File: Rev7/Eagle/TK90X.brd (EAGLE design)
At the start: 217.8 x 132.1 mm, 224 parts, among them IC1 Z80, IC10 74LS244N, IC11 LM1886, IC12 LM1889, IC13 4116, IC14 4116, IC15 4116, IC16 4116, IC17 4116, IC18 4116, IC19 4116, IC2 ROM, IC20 4116, IC21 4416, IC22 4416, IC23 4416, IC24 4416, IC25 74LS00, IC26 74LS00, IC27 74LS32, IC28 74LS04, IC29 7805, IC3 ULA TK90, IC4 74LS74, IC5 74LS74, IC6 74LS157, IC7 74LS157, IC8 74LS157, IC9 74LS157, Q1 BC548, Q2 BC548, Q3 BF494, Q4 BC548, Q5 BD139, Q6 BD136, Q7 BC548, Q8 BC517, X1 POWER, X2 EAR, X3 MIC, X4 RCA, X5 RCA, X6 LED, X7 JOYSTICK

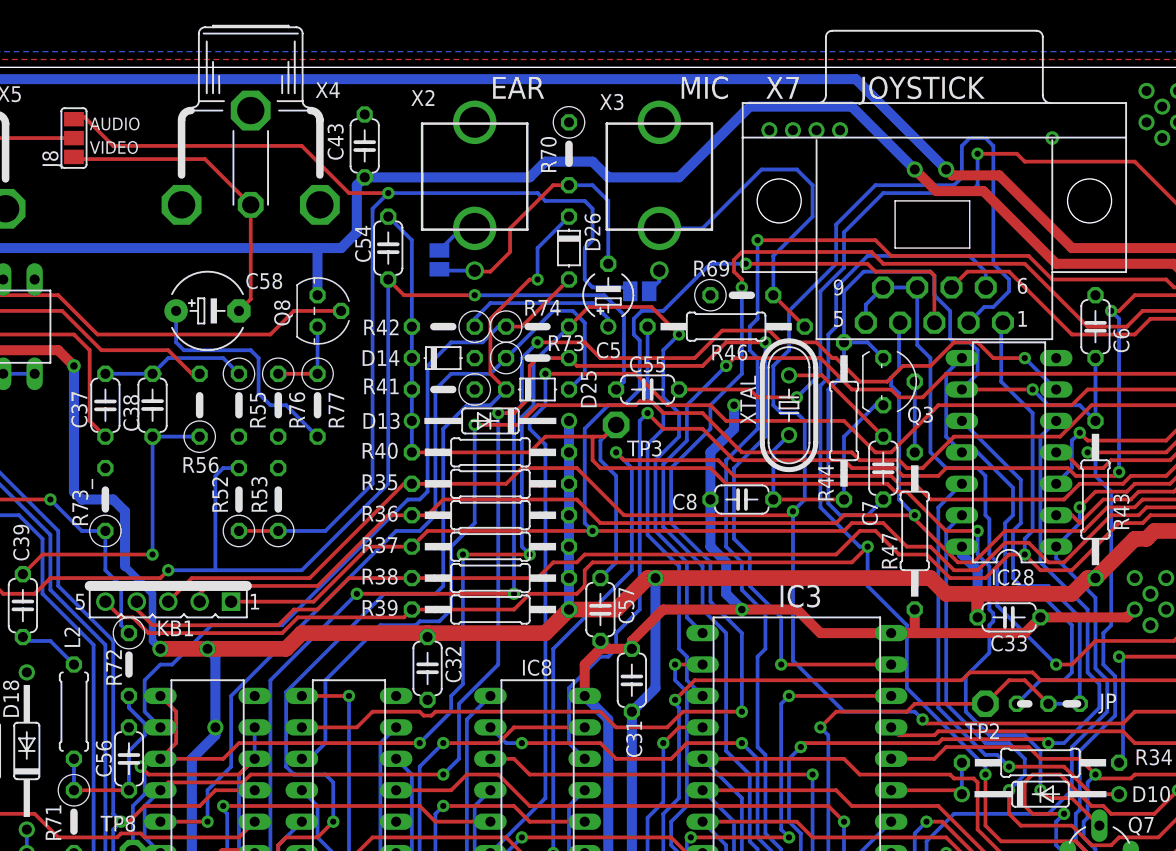
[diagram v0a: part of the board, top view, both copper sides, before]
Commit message: Corrigido valor de R49 e outros pequenos detalhes
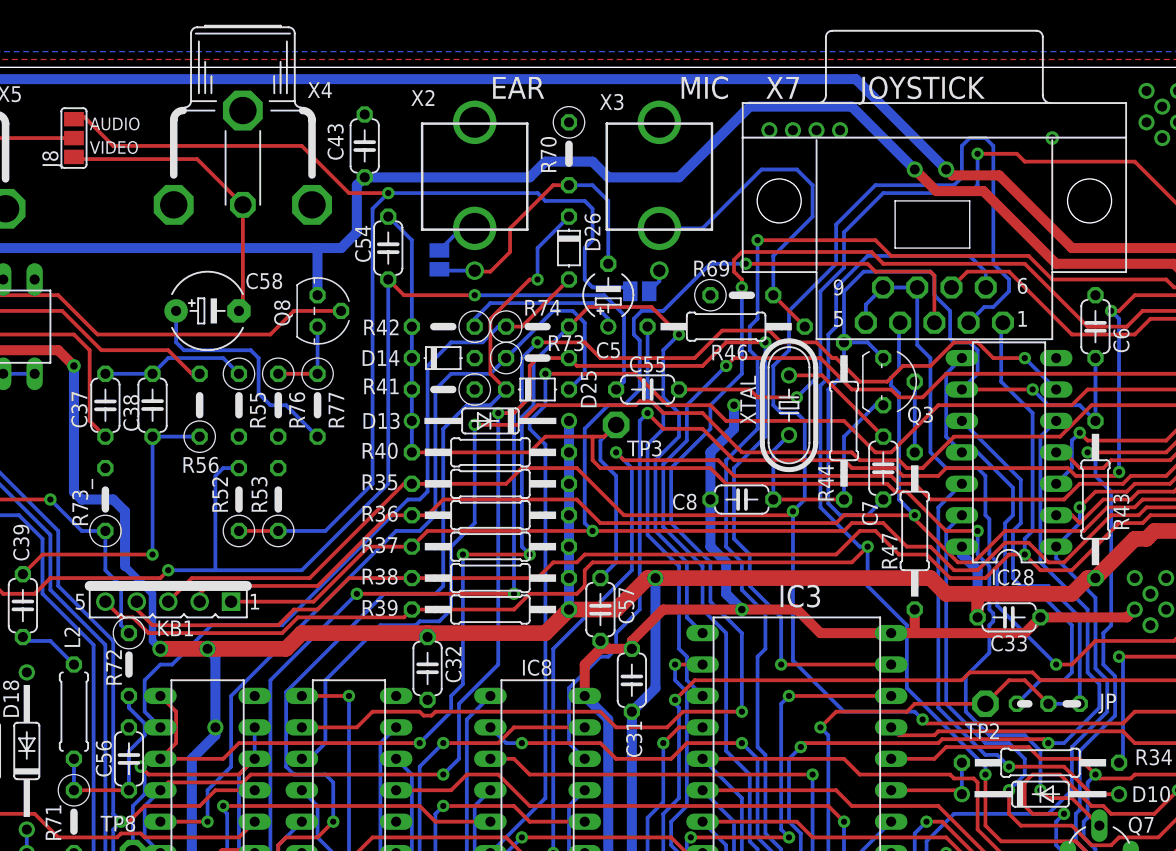
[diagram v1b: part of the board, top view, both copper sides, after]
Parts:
- R49: value 1K -> 4K7
- moved X4 0.64 mm to (42.9, 123.5)
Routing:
- net VIDEO: track 24.9 -> 24.0 mm
- net N$82: track 12.5 -> 11.8 mm

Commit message: Pequenas correções
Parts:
- C1: value 10V100u -> 10V1000u
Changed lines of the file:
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@@
 </autorouter>
 <elements>
-<element name="C1" library="rcl" package="E5-5" value="10V100u" x="203.2" y="83.82" smashed="yes" rot="R90">
+<element name="C1" library="rcl" package="E5-5" value="10V1000u" x="203.2" y="83.82" smashed="yes" rot="R90">
 <attribute name="NAME" x="202.5777" y="88.9635" size="1.27" layer="25" ratio="10"/>
 <attribute name="VALUE" x="206.2226" y="81.3054" size="1.27" layer="27" ratio="10" rot="R90"/>

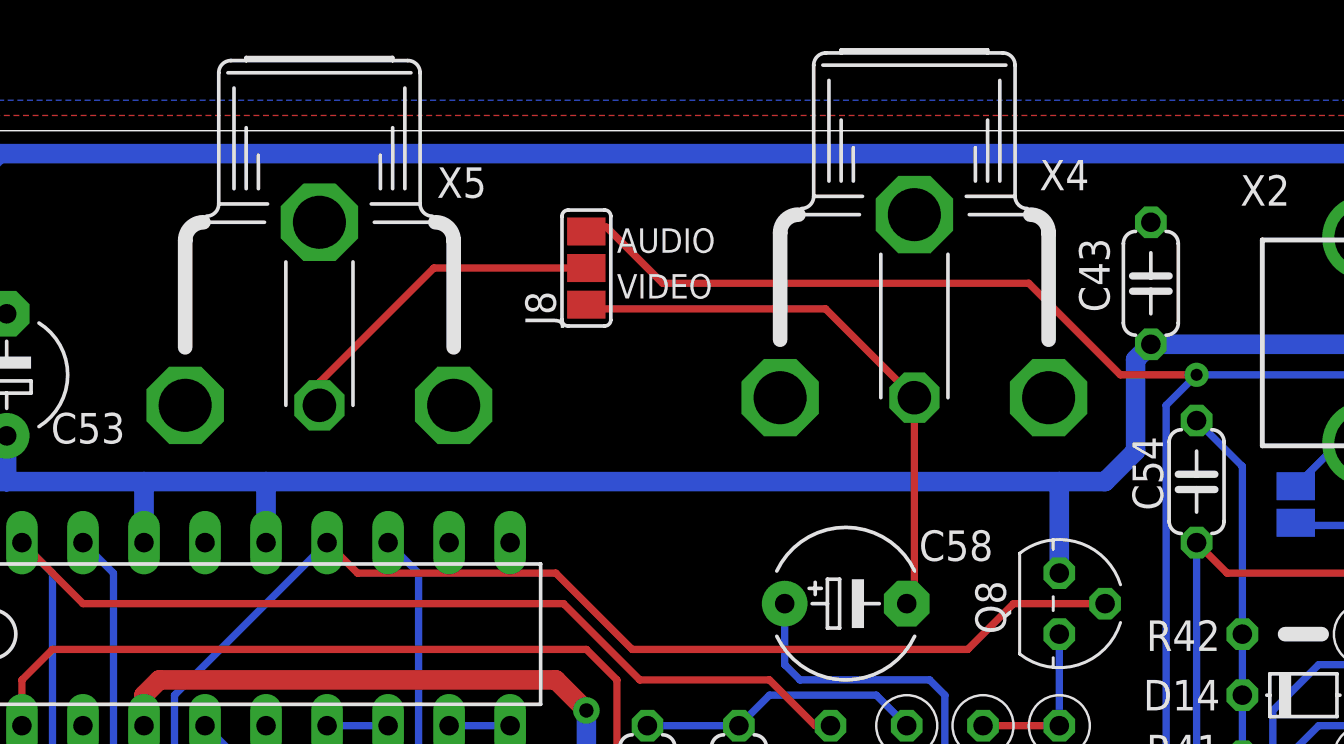
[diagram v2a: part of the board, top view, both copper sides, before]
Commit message: Corrigindo footprint dos jacks RCA Corrigindo lista de peças da revisão 7
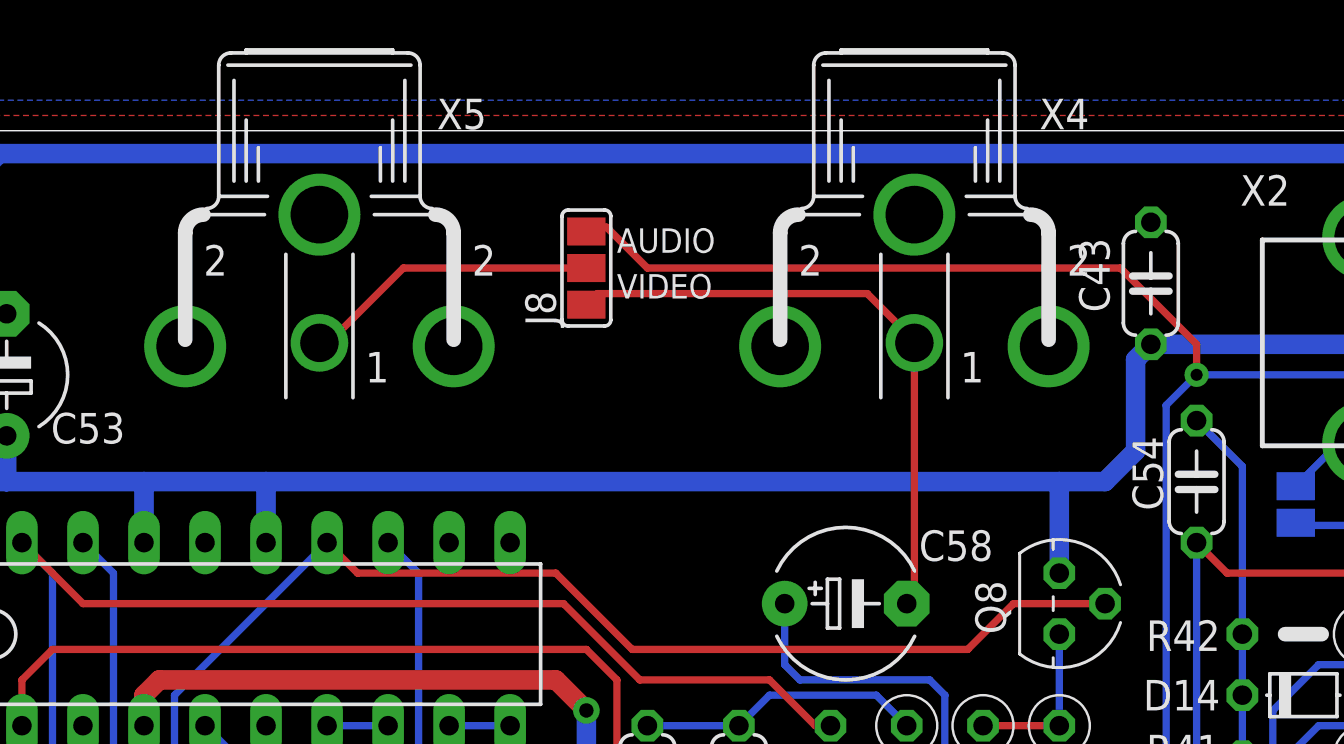
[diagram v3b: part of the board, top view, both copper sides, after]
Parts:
- X4, X5: device tk90:TOBU3 -> tk90:DX1
- moved X5 2.86 mm to (18.1, 126.0)
- moved X4 2.54 mm to (42.9, 126.0)
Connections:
- net !ROMCS: now also TP9.TP; no longer TP9.1
- net !VCAS: now also TP5.TP; no longer TP5.1
- net !VRAS: now also TP4.TP; no longer TP4.1
- net !VWR: now also TP6.TP; no longer TP6.1
- net /INT: now also TP10.TP; no longer TP10.1
- net BEEP: now also TP7.TP; no longer TP7.1
- net GND: now also X4.2, X4.2@1, X4.2@2, X5.2, X5.2@1, X5.2@2; no longer X4.SHELL, X4.SHELL@1, X4.SHELL@2, X5.SHELL, X5.SHELL@1, X5.SHELL@2
- net N$47: now also TP2.TP; no longer TP2.1
- net N$54: now also TP8.TP; no longer TP8.1
- net N$74: now also X5.1; no longer X5.PIN
- net SNDIN: now also TP3.TP; no longer TP3.1
- net VIDEO: now also X4.1; no longer X4.PIN
- net Z80CLK: now also TP1.TP; no longer TP1.1
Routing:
- net VIDEO: track 24.0 -> 25.7 mm
- net N$74: track 14.0 -> 12.4 mm
- net AUDIO: track 91.5 -> 92.2 mm

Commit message: Adicionado fotos da placa Rev 7 montada Alterado instruções para formato Markdown Corrigido capacitor C1 na placa rev. 7 Outras pequenas melhorias e correções
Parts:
- C1: device rcl:E5-5 -> rcl:E5-8,5
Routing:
- net +5V: track 1091.5 -> 1090.8 mm
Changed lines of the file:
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@@
 </autorouter>
 <elements>
-<element name="C1" library="rcl" package="E5-5" value="10V1000u" x="203.2" y="83.82" smashed="yes" rot="R90">
+<element name="C1" library="rcl" package="E5-8,5" value="10V1000u" x="203.2" y="83.82" smashed="yes" rot="R90">
 <attribute name="NAME" x="202.5777" y="88.9635" size="1.27" layer="25" ratio="10"/>
 <attribute name="VALUE" x="206.2226" y="81.3054" size="1.27" layer="27" ratio="10" rot="R90"/>
@@
 <attribute name="NAME" x="107.696" y="65.7225" size="1.27" layer="25" ratio="10" rot="R180"/>
 <attribute name="POPULARITY" value="0" x="106.68" y="66.9925" size="1.778" layer="27" rot="R180" display="off"/>
+<attribute name="TP_SIGNAL_NAME" value="" x="106.68" y="66.9925" size="1.778" layer="27" rot="R180" display="off"/>
 <attribute name="TP_SIGNAL_NAME" value="" x="107.95" y="69.5325" size="1" layer="37" rot="R180"/>
-<attribute name="TP_SIGNAL_NAME" value="" x="106.68" y="66.9925" size="1.778" layer="27" rot="R180" display="off"/>
 <attribute name="VALUE" x="106.68" y="66.9925" size="0.0254" layer="27" rot="R180"/>
 </element>
@@
 <attribute name="NAME" x="149.7965" y="116.84" size="1.27" layer="25" ratio="10"/>
 <attribute name="POPULARITY" value="0" x="153.035" y="119.38" size="1.778" layer="27" rot="R180" display="off"/>
+<attribute name="TP_SIGNAL_NAME" value="" x="153.035" y="119.38" size="1.778" layer="27" rot="R180" display="off"/>
 <attribute name="TP_SIGNAL_NAME" value="" x="154.305" y="121.92" size="1" layer="37" rot="R180"/>
-<attribute name="TP_SIGNAL_NAME" value="" x="153.035" y="119.38" size="1.778" layer="27" rot="R180" display="off"/>
 <attribute name="VALUE" x="153.035" y="119.38" size="0.0254" layer="27" rot="R180"/>
 </element>
@@
 <attribute name="NAME" x="91.821" y="4.7625" size="1.27" layer="25" ratio="10" rot="R180"/>
 <attribute name="POPULARITY" value="0" x="90.17" y="6.35" size="1.778" layer="27" rot="R180" display="off"/>
+<attribute name="TP_SIGNAL_NAME" value="" x="90.17" y="6.35" size="1.778" layer="27" rot="R180" display="off"/>
 <attribute name="TP_SIGNAL_NAME" value="" x="91.44" y="8.89" size="1" layer="37" rot="R180"/>
-<attribute name="TP_SIGNAL_NAME" value="" x="90.17" y="6.35" size="1.778" layer="27" rot="R180" display="off"/>
 <attribute name="VALUE" x="90.17" y="6.35" size="0.0254" layer="27" rot="R180"/>
 </element>
@@
 <attribute name="NAME" x="84.201" y="4.7625" size="1.27" layer="25" ratio="10" rot="R180"/>
 <attribute name="POPULARITY" value="0" x="82.55" y="6.35" size="1.778" layer="27" rot="R180" display="off"/>
+<attribute name="TP_SIGNAL_NAME" value="" x="82.55" y="6.35" size="1.778" layer="27" rot="R180" display="off"/>
 <attribute name="TP_SIGNAL_NAME" value="" x="83.82" y="8.89" size="1" layer="37" rot="R180"/>
-<attribute name="TP_SIGNAL_NAME" value="" x="82.55" y="6.35" size="1.778" layer="27" rot="R180" display="off"/>
 <attribute name="VALUE" x="82.55" y="6.35" size="0.0254" layer="27" rot="R180"/>
 </element>
@@
 <attribute name="NAME" x="88.011" y="4.7625" size="1.27" layer="25" ratio="10" rot="R180"/>
 <attribute name="POPULARITY" value="0" x="86.36" y="6.35" size="1.778" layer="27" rot="R180" display="off"/>
+<attribute name="TP_SIGNAL_NAME" value="" x="86.36" y="6.35" size="1.778" layer="27" rot="R180" display="off"/>
 <attribute name="TP_SIGNAL_NAME" value="" x="87.63" y="8.89" size="1" layer="37" rot="R180"/>
-<attribute name="TP_SIGNAL_NAME" value="" x="86.36" y="6.35" size="1.778" layer="27" rot="R180" display="off"/>
 <attribute name="VALUE" x="86.36" y="6.35" size="0.0254" layer="27" rot="R180"/>
 </element>
@@
 <attribute name="NAME" x="40.7035" y="45.72" size="1.27" layer="25" ratio="10" rot="R180"/>
 <attribute name="POPULARITY" value="0" x="39.6875" y="46.99" size="1.778" layer="27" rot="R180" display="off"/>
+<attribute name="TP_SIGNAL_NAME" value="" x="39.6875" y="46.99" size="1.778" layer="27" rot="R180" display="off"/>
 <attribute name="TP_SIGNAL_NAME" value="" x="40.9575" y="49.53" size="1" layer="37" rot="R180"/>
-<attribute name="TP_SIGNAL_NAME" value="" x="39.6875" y="46.99" size="1.778" layer="27" rot="R180" display="off"/>
 <attribute name="VALUE" x="39.6875" y="46.99" size="0.0254" layer="27" rot="R180"/>
 </element>
@@
 <attribute name="NAME" x="101.219" y="77.7875" size="1.27" layer="25" ratio="10"/>
 <attribute name="POPULARITY" value="0" x="102.87" y="80.645" size="1.778" layer="27" display="off"/>
+<attribute name="TP_SIGNAL_NAME" value="" x="102.87" y="80.645" size="1.778" layer="27" display="off"/>
 <attribute name="TP_SIGNAL_NAME" value="" x="101.6" y="78.105" size="1" layer="37"/>
-<attribute name="TP_SIGNAL_NAME" value="" x="102.87" y="80.645" size="1.778" layer="27" display="off"/>
 <attribute name="VALUE" x="102.87" y="80.645" size="0.0254" layer="27"/>
 </element>
@@
 <attribute name="NAME" x="73.914" y="100.6475" size="1.27" layer="25" ratio="10"/>
 <attribute name="POPULARITY" value="0" x="73.025" y="103.1875" size="1.778" layer="27" display="off"/>
+<attribute name="TP_SIGNAL_NAME" value="" x="73.025" y="103.1875" size="1.778" layer="27" display="off"/>
 <attribute name="TP_SIGNAL_NAME" value="" x="71.755" y="100.6475" size="1" layer="37"/>
-<attribute name="TP_SIGNAL_NAME" value="" x="73.025" y="103.1875" size="1.778" layer="27" display="off"/>
 <attribute name="VALUE" x="73.025" y="103.1875" size="0.0254" layer="27"/>
 </element>
@@
 <attribute name="NAME" x="187.6425" y="55.499" size="1.27" layer="25" ratio="10" rot="R90"/>
 <attribute name="POPULARITY" value="0" x="184.785" y="57.15" size="1.778" layer="27" display="off"/>
+<attribute name="TP_SIGNAL_NAME" value="" x="184.785" y="57.15" size="1.778" layer="27" display="off"/>
 <attribute name="TP_SIGNAL_NAME" value="" x="183.515" y="54.61" size="1" layer="37"/>
-<attribute name="TP_SIGNAL_NAME" value="" x="184.785" y="57.15" size="1.778" layer="27" display="off"/>
 <attribute name="VALUE" x="184.785" y="57.15" size="0.0254" layer="27"/>
 </element>
@@
 <attribute name="NAME" x="31.369" y="70.32625" size="1.27" layer="25" font="vector" ratio="10"/>
 <attribute name="POPULARITY" value="0" x="33.9725" y="68.58" size="1.778" layer="27" display="off"/>
+<attribute name="TP_SIGNAL_NAME" value="" x="33.9725" y="68.58" size="1.778" layer="27" display="off"/>
 <attribute name="TP_SIGNAL_NAME" value="" x="32.7025" y="66.04" size="1" layer="37"/>
-<attribute name="TP_SIGNAL_NAME" value="" x="33.9725" y="68.58" size="1.778" layer="27" display="off"/>
 <attribute name="VALUE" x="33.9725" y="68.58" size="0.0254" layer="27"/>
 </element>
@@
 <wire x1="200.025" y1="93.345" x2="191.77" y2="93.345" width="1.9304" layer="16"/>
 <wire x1="191.77" y1="93.345" x2="189.865" y2="93.345" width="1.9304" layer="16"/>
-<wire x1="200.025" y1="82.8675" x2="200.025" y2="93.345" width="1.27" layer="16"/>
+<wire x1="200.025" y1="84.1375" x2="200.025" y2="93.345" width="1.27" layer="16"/>
 <via x="191.77" y="93.345" extent="1-16" drill="0.8"/>
 <wire x1="166.37" y1="65.405" x2="166.37" y2="67.945" width="0.8128" layer="16"/>
@@
 <wire x1="209.55" y1="76.835" x2="212.725" y2="76.835" width="1.27" layer="16"/>
 <wire x1="212.725" y1="76.835" x2="213.995" y2="75.565" width="1.27" layer="16"/>
-<wire x1="200.025" y1="82.8675" x2="201.6125" y2="81.28" width="1.27" layer="16"/>
-<wire x1="201.6125" y1="81.28" x2="203.2" y2="81.28" width="1.27" layer="16"/>
+<wire x1="200.025" y1="84.1375" x2="202.8825" y2="81.28" width="1.27" layer="16"/>
+<wire x1="202.8825" y1="81.28" x2="203.2" y2="81.28" width="1.27" layer="16"/>
 <wire x1="203.2" y1="81.28" x2="207.01" y2="81.28" width="1.27" layer="16"/>
 <wire x1="207.01" y1="81.28" x2="209.55" y2="78.74" width="1.27" layer="16"/>
